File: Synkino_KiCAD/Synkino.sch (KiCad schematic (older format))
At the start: 155 parts, among them J1 Conn_01x02_Male, J10 EYE8_OUT, J11 EYE4_OUT, J12 2.5mm, J13 EYE5_OUT, J2 2.5mm, J3 3.5mm, J4 Micro_SD_Card_Det_Hirose_DM3AT, J5 EYE1_OUT, J6 EYE6_OUT, J7 EYE2_OUT, J8 EYE7_OUT, J9 EYE3_OUT, Q1 IRF7319, Q2 BC847, SW1 SW_Push, SW2 Rotary_Encoder_Switch, SW3 SW_Push, U1 MCP1702T-5002E/MB, U10 ATMEGA328P-AU, U11 QRE1113, U12 QRE1113, U13 QRE1113, U14 QRE1113, U15 QRE1113, U16 QRE1113, U18 QRE1113, U2 ATMEGA328P-AU, U3 74HC4050, U4 SPIOLED128x64, U5 AP7312-1833W6-7, U6 74HC14, U7 VS1053B, U8 MAX4741, U9 QRE1113, X1 FTDIconn, X2 ICSP, X3 FTDIconn, X4 ICSP, Y1 16Mhz, Y2 12.288MHz, Y3 16Mhz

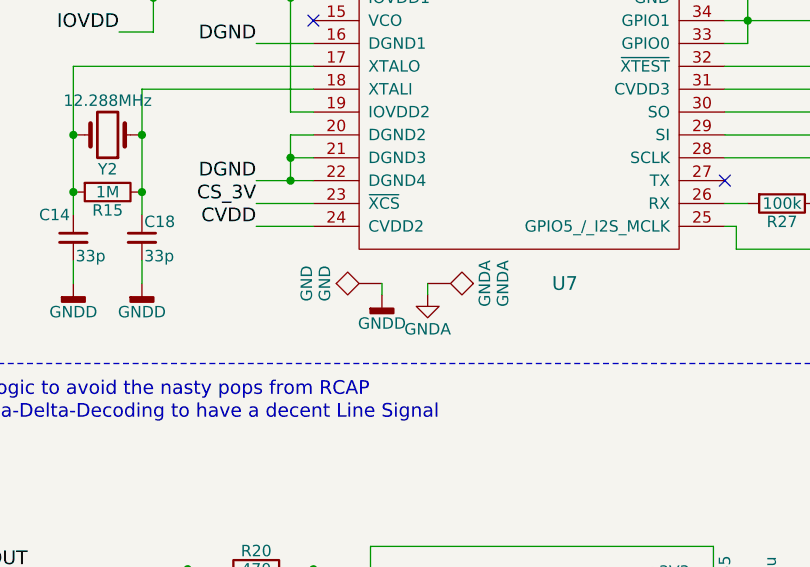
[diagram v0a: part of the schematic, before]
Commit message: More Ground Planes, Make Pwr Button optional
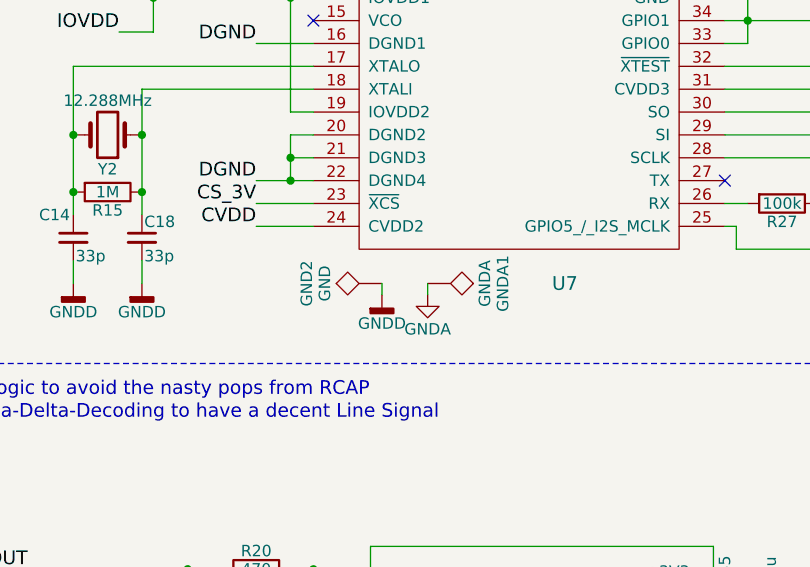
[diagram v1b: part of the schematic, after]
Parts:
- GND2: renamed from GND; footprint (none) -> Measurement_Points:Measurement_Point_Square-SMD-Pad_Small
- GNDA1: renamed from GNDA; footprint (none) -> Measurement_Points:Measurement_Point_Square-SMD-Pad_Small
- U1: footprint TO_SOT_Packages_SMD:SOT-23 -> TO_SOT_Packages_SMD:SOT-89-3_Handsoldering
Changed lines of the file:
@@
 F 0 "U1" H 1400 1375 50  0000 C CNN
 F 1 "MCP1702T-5002E/MB" H 1550 1375 50  0000 L CNN
-F 2 "TO_SOT_Packages_SMD:SOT-23" H 1550 1450 50  0001 C CNN
+F 2 "TO_SOT_Packages_SMD:SOT-89-3_Handsoldering" H 1550 1450 50  0001 C CNN
 F 3 "" H 1550 1200 50  0001 C CNN
 	1    1550 1250
@@
 	15200 4950 15300 4950
 $Comp
-L TEST GNDA
+L TEST GNDA1
 U 1 1 5AAC2C8C
 P 8250 4800
-F 0 "GNDA" H 8250 5100 50  0000 C BNN
+F 0 "GNDA1" H 8250 5100 50  0000 C BNN
 F 1 "GNDA" H 8250 5050 50  0000 C CNN
-F 2 "" H 8250 4800 50  0001 C CNN
+F 2 "Measurement_Points:Measurement_Point_Square-SMD-Pad_Small" H 8250 4800 50  0001 C CNN
 F 3 "" H 8250 4800 50  0001 C CNN
 	1    8250 4800
@@
 $EndComp
 $Comp
-L TEST GND
+L TEST GND2
 U 1 1 5AAC2E8C
 P 8050 4800
-F 0 "GND" H 8050 5100 50  0000 C BNN
+F 0 "GND2" H 8050 5100 50  0000 C BNN
 F 1 "GND" H 8050 5050 50  0000 C CNN
-F 2 "" H 8050 4800 50  0001 C CNN
+F 2 "Measurement_Points:Measurement_Point_Square-SMD-Pad_Small" H 8050 4800 50  0001 C CNN
 F 3 "" H 8050 4800 50  0001 C CNN
 	1    8050 4800

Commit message: Kalle safe :)
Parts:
- U8: footprint TO_SOT_Packages_SMD:SOT-23-8_Handsoldering -> Housings_SSOP:MSOP-8_3x3mm_Pitch0.65mm
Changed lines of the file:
@@
 F 0 "U8" H 8800 6150 60  0000 C CNN
 F 1 "MAX4741" H 8800 7100 60  0000 C CNN
-F 2 "TO_SOT_Packages_SMD:SOT-23-8_Handsoldering" H 8900 6550 60  0001 C CNN
+F 2 "Housings_SSOP:MSOP-8_3x3mm_Pitch0.65mm" H 8900 6550 60  0001 C CNN
 F 3 "" H 8900 6550 60  0001 C CNN
 	1    8800 6600

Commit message: Fix LDO pinout bug :(
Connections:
- net at C5.1, R6.2: now also C6.1, Q1.4 (G2), Q1.8 (D1)
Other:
- moved on the sheet: C5, C6, C9, R2, SW1

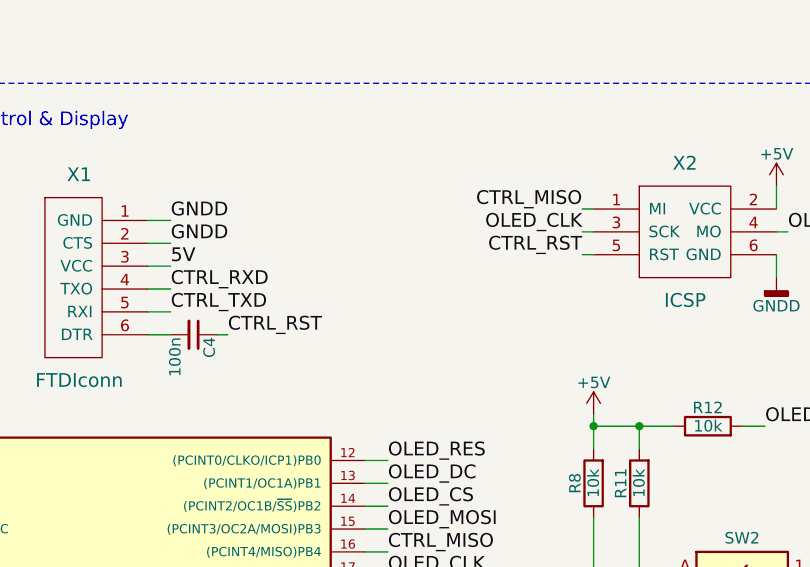
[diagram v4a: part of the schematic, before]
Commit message: Fixing Reset (partially)
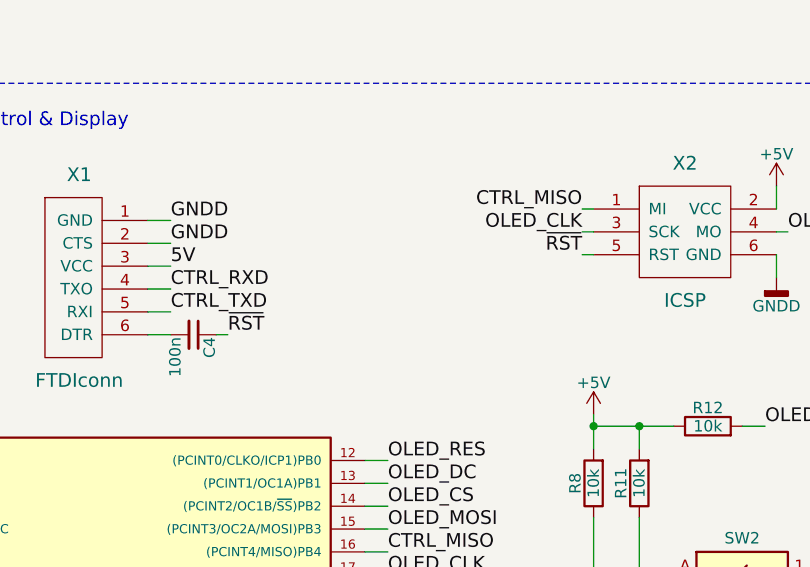
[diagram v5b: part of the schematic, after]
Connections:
- net CTRL_RST is gone; now on net ~RST: C4.1, X2.5 (RST)
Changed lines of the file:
@@
 Text Label 2950 8250 0    60   ~ 0
 ~RST
-Text Label 3800 5900 2    60   ~ 0
-CTRL_RST
 $Comp
 L R R12
@@
 	0    1    1    0
 $EndComp
-Text Label 2250 6250 0    60   ~ 0
-CTRL_RST
 Text Label 2950 8500 0    60   ~ 0
 CTRL_TXD
@@
 Wire Wire Line
 	1850 1250 3000 1250
+Text Label 3800 5900 2    60   ~ 0
+~RST
+Text Label 2250 6250 0    60   ~ 0
+~RST
 $EndSCHEMATC

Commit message: Minor Schematic Tweaks
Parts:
- R30: value 270 -> 330
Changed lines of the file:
@@
 P 9950 9650
 F 0 "R30" V 10030 9650 50  0000 C CNN
-F 1 "270" V 9950 9650 50  0000 C CNN
+F 1 "330" V 9950 9650 50  0000 C CNN
 F 2 "Resistors_SMD:R_0805_HandSoldering" V 9880 9650 50  0001 C CNN
 F 3 "" H 9950 9650 50  0001 C CNN

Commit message: Reverse Polarity Protection Tweaks
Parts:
- removed JP1: (no value), Pin_Headers:Pin_Header_Straight_1x02_Pitch2.54mm, symbol Jumper_NC_Small
- added D?: BZX84C9V1, symbol D_Zener_Small
- added Q?: IRLML2244, SOT-23, symbol IRLML2244
- added R?: 100k, Resistors_SMD:R_0805_HandSoldering, symbol R
- J1: value Conn_01x02_Male -> Pwr
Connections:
- net GND: now also R?.1
- net MISO_3V: now also U10.16 ((PCINT4/MISO)PB4)
- net at C2.1, U1.2 (VI): now also D?.1 (K), Q?.2 (S); no longer J1.1 (Pin_1)
- new net: J1.1 (Pin_1), Q?.3 (D)
- new net: D?.2 (A), Q?.1 (G), R?.2
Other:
- note added: "Level Shifter, VS1053 likes 3v3 only, Mega328 needs 5V for 16 MHz"
- note removed: "Level Shifter, VS1053 likes 3v3 only, Mega328 needs 5V though for 16 MHz"
- moved on the sheet: C10, C11, C12, C2, C3, C5, C6, C9, D1, J1, Q1, R1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

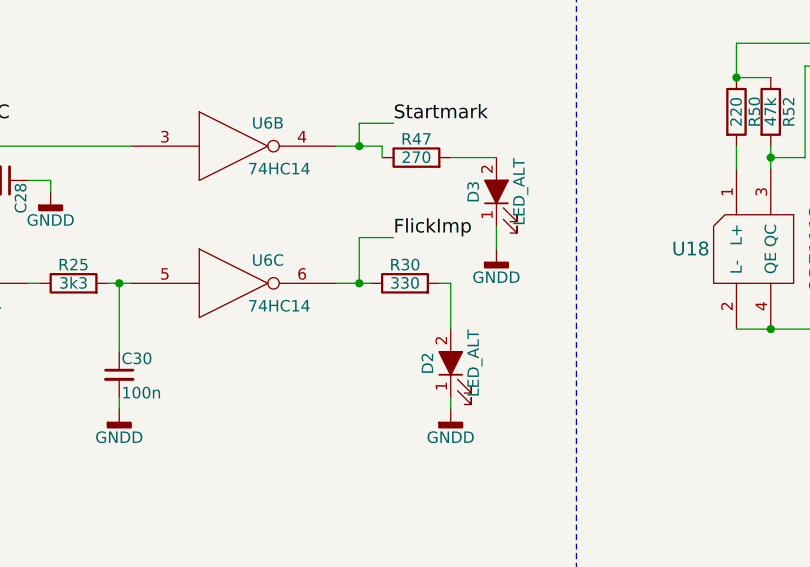
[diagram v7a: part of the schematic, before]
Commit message: Polarity Protection
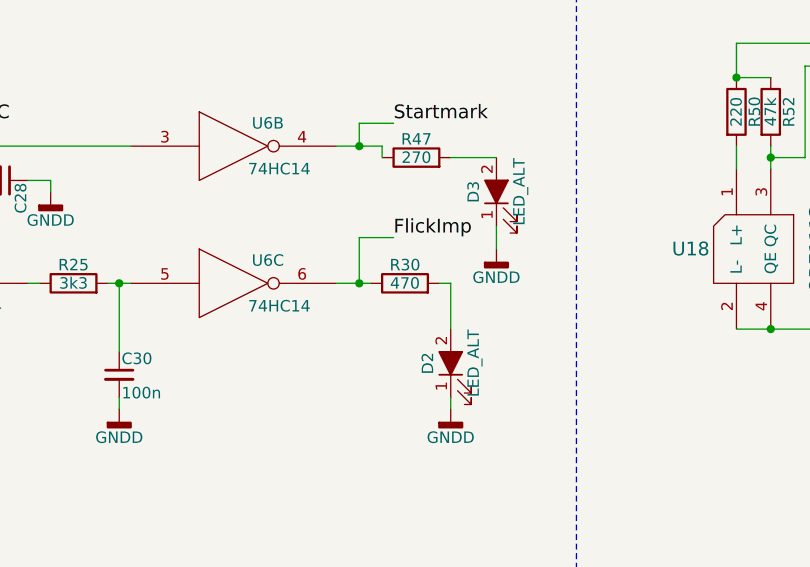
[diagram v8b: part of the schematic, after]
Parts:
- R30: value 330 -> 470
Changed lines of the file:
@@
 P 9950 9650
 F 0 "R30" V 10030 9650 50  0000 C CNN
-F 1 "330" V 9950 9650 50  0000 C CNN
+F 1 "470" V 9950 9650 50  0000 C CNN
 F 2 "Resistors_SMD:R_0805_HandSoldering" V 9880 9650 50  0001 C CNN
 F 3 "" H 9950 9650 50  0001 C CNN
